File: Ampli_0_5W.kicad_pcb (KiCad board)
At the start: 2 copper layers, 100 x 100 mm, 66 parts, among them J1 RF_In, J2 PTT_In, J3 Aux_PTT_Out, J4 RF_Out, Q1 2N7002, Q2 FDD6685, Q3 2N5109, Q4 AFT05MP075N, T1 4:1, T2 1:1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

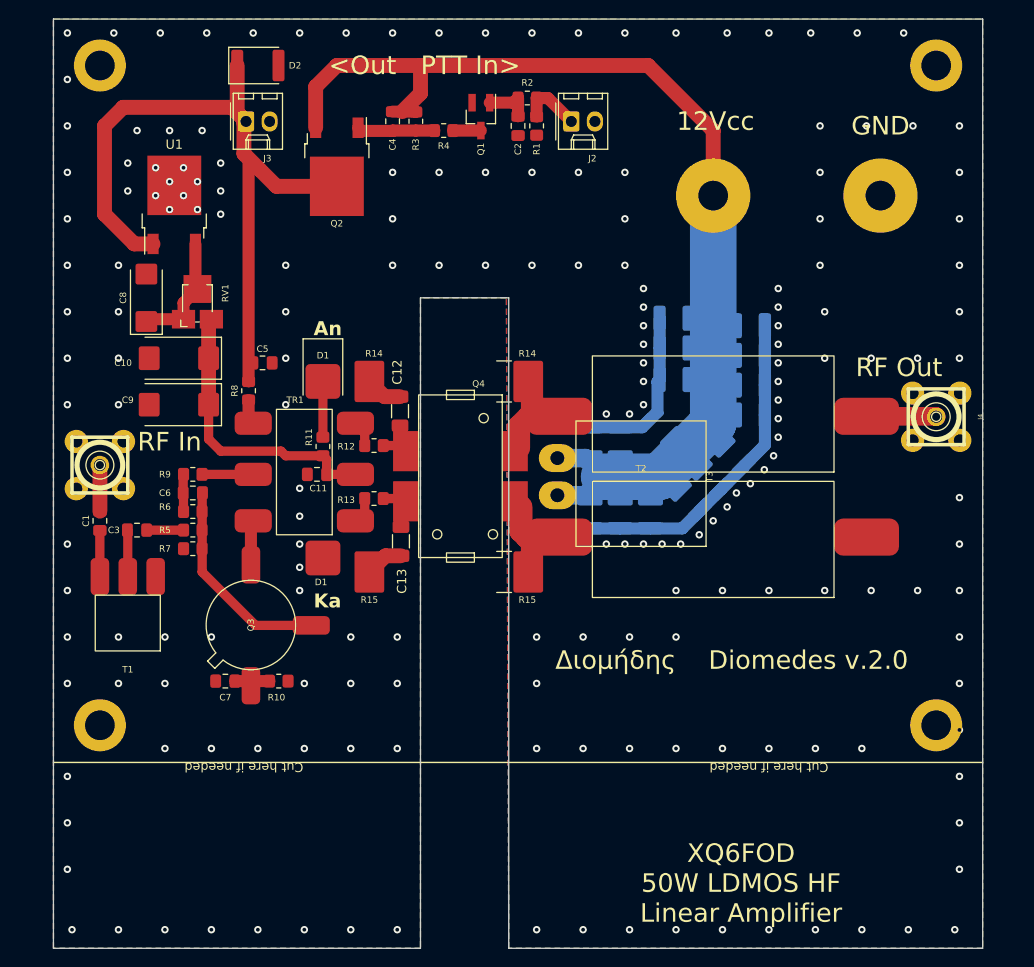
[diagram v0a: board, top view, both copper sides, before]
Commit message: pennywhistle compatible mounting holes
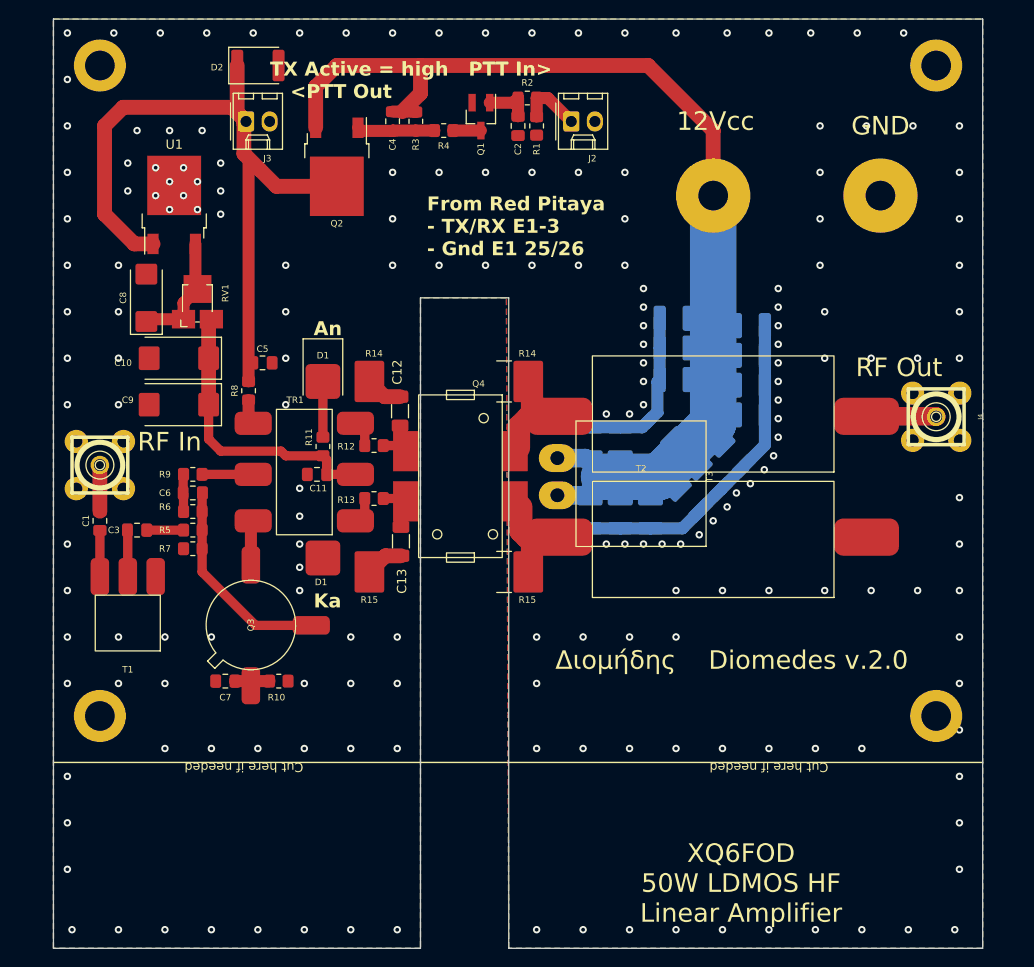
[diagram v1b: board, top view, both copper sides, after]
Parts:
- moved H4 1.00 mm to (85.0, 105.0)
- moved H6 1.00 mm to (175.0, 105.0)
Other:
- board text added: "From Red Pitaya - TX/RX E1-3 - Gnd E1 25/26"
- board text added: "TX Active = high PTT In> <PTT Out"
- board text removed: "<Out PTT In>"
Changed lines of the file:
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@@
   )
   (footprint "MountingHole:MountingHole_3.2mm_M3_DIN965_Pad" (layer "F.Cu")
-    (at 85 106)
+    (at 85 105)
     (descr "Mounting Hole 3.2mm, M3, DIN965")
     (tags "mounting hole 3.2mm m3 din965")
@@
     (property "ki_keywords" "diode")
     (attr smd)
-    (fp_text reference "D2" (at 4 0) (layer "F.SilkS")
+    (fp_text reference "D2" (at -4.4 0.2) (layer "F.SilkS")
         (effects (font (size 0.7 0.7) (thickness 0.15)))
     )
@@
   )
   (footprint "MountingHole:MountingHole_3.2mm_M3_DIN965_Pad" (layer "F.Cu")
-    (at 175 106)
+    (at 175 105)
     (descr "Mounting Hole 3.2mm, M3, DIN965")
     (tags "mounting hole 3.2mm m3 din965")
@@
     (effects (font (size 0.7 0.7) (thickness 0.15)))
   )
-  (gr_text " <Out   PTT In>" (at 119.5 35) (layer "F.SilkS")
-    (effects (font (size 2 2) (thickness 0.375)))
+  (gr_text "                      TX Active = high   PTT In>\n <PTT Out  " (at 110.6 36.6) (layer "F.SilkS")
+    (effects (font (size 1.5 1.5) (thickness 0.3) bold))
   )
   (gr_text "RF Out" (at 171 67.5) (layer "F.SilkS")
@@
     (effects (font (size 2 2) (thickness 0.4)))
   )
+  (gr_text "From Red Pitaya \n- TX/RX E1-3\n- Gnd E1 25/26" (at 120.2 55.6) (layer "F.SilkS")
+    (effects (font (size 1.5 1.5) (thickness 0.3) bold) (justify left bottom))
+  )
   (gr_text "Cut here if needed" (at 100.5 110.5 180) (layer "F.SilkS")
     (effects (font (size 1 1) (thickness 0.15)))
@@
     (effects (font (size 2 2) (thickness 0.4)))
   )
-  (dimension (type aligned) (layer "B.Cu")
-    (pts (xy 128.9 130) (xy 129.1 100))
-    (height -3.996577)
-    (gr_text "30.0007 mm" (at 123.203552 114.961357 89.6180338) (layer "B.Cu")
-      (effects (font (size 1.5 1.5) (thickness 0.3)))
+  (dimension (type aligned) (layer "F.SilkS")
+    (pts (xy 175 35) (xy 175 105))
+    (height -20)
+    (gr_text "70.0000 mm" (at 193.85 70 90) (layer "F.SilkS")
+      (effects (font (size 1 1) (thickness 0.15)))
     )
     (format (prefix "") (suffix "") (units 3) (units_format 1) (precision 4))
-    (style (thickness 0.2) (arrow_length 1.27) (text_position_mode 0) (extension_height 0.58642) (extension_offset 0.5) keep_text_aligned)
-  )
-  (dimension (type aligned) (layer "B.Cu")
-    (pts (xy 129 130) (xy 180 130))
-    (height 5.2)
-    (gr_text "51.0000 mm" (at 154.5 133.4) (layer "B.Cu")
-      (effects (font (size 1.5 1.5) (thickness 0.3)))
+    (style (thickness 0.15) (arrow_length 1.27) (text_position_mode 0) (extension_height 0.58642) (extension_offset 0.5) keep_text_aligned)
+  )
+  (dimension (type aligned) (layer "F.SilkS")
+    (pts (xy 85 35) (xy 175 35))
+    (height -20)
+    (gr_text "90.0000 mm" (at 130 13.85) (layer "F.SilkS")
+      (effects (font (size 1 1) (thickness 0.15)))
     )
     (format (prefix "") (suffix "") (units 3) (units_format 1) (precision 4))
-    (style (thickness 0.2) (arrow_length 1.27) (text_position_mode 0) (extension_height 0.58642) (extension_offset 0.5) keep_text_aligned)
+    (style (thickness 0.15) (arrow_length 1.27) (text_position_mode 0) (extension_height 0.58642) (extension_offset 0.5) keep_text_aligned)
   )
   (segment (start 85 78) (end 85 82.9625) (width 1.6) (layer "F.Cu") (net 1))

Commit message: new 3D image, minor changes
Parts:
- added C30: 100n, Capacitor_SMD:C_0603_1608Metric_Pad1.08x0.95mm_HandSolder, F.Cu at (105.5, 92.5)
- added Q5: 2SC5551A, Package_TO_SOT_SMD:SOT-89-3, F.Cu at (101.0, 90.6)
- added R16: 10R, Resistor_SMD:R_0603_1608Metric_Pad0.98x0.95mm_HandSolder, F.Cu at (105.5, 91.0)
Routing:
- net Net-(Q3-B): track 22.6 -> 32.0 mm
- net Net-(Q3-C): track 4.85 -> 0.35 mm
- net Net-(Q5-E): track 0.00 -> 3.69 mm
- net GND: track 52.7 -> 54.9 mm, vias 185 -> 213

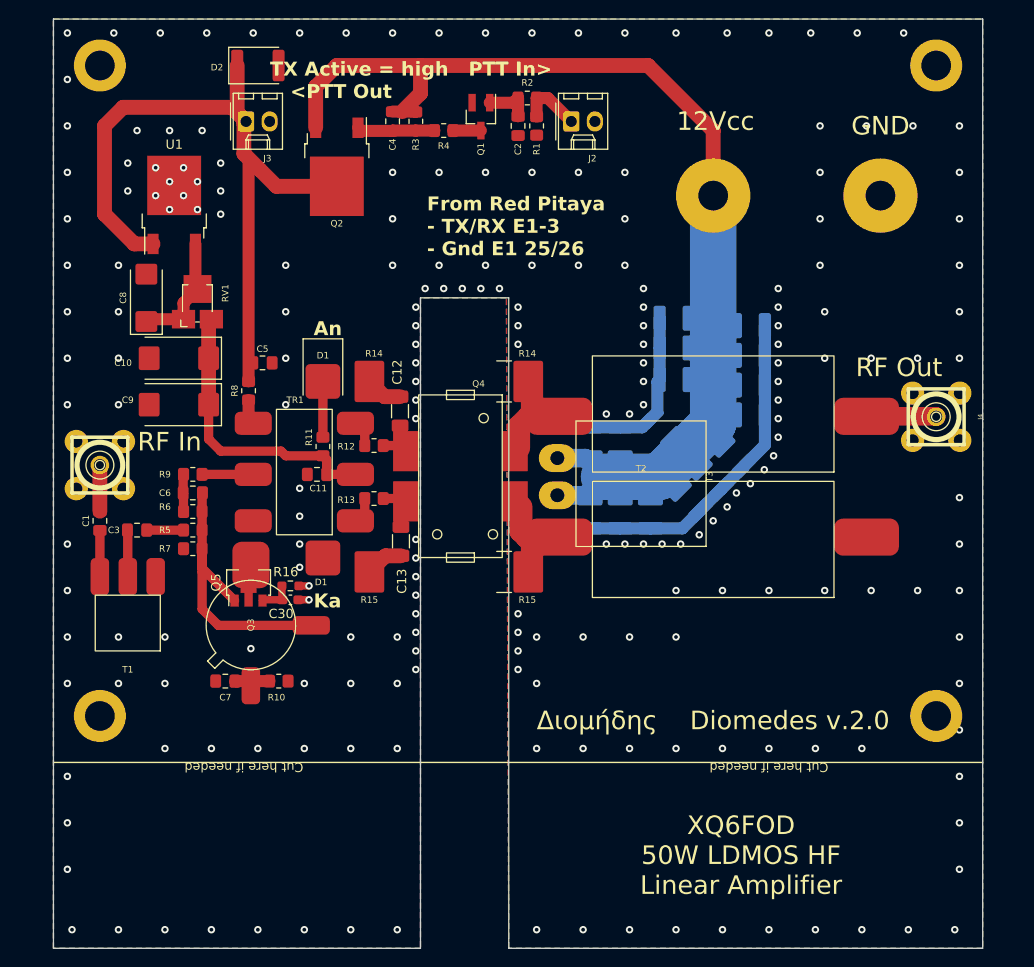
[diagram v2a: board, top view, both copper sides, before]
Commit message: new slotted pcb, new transistor added
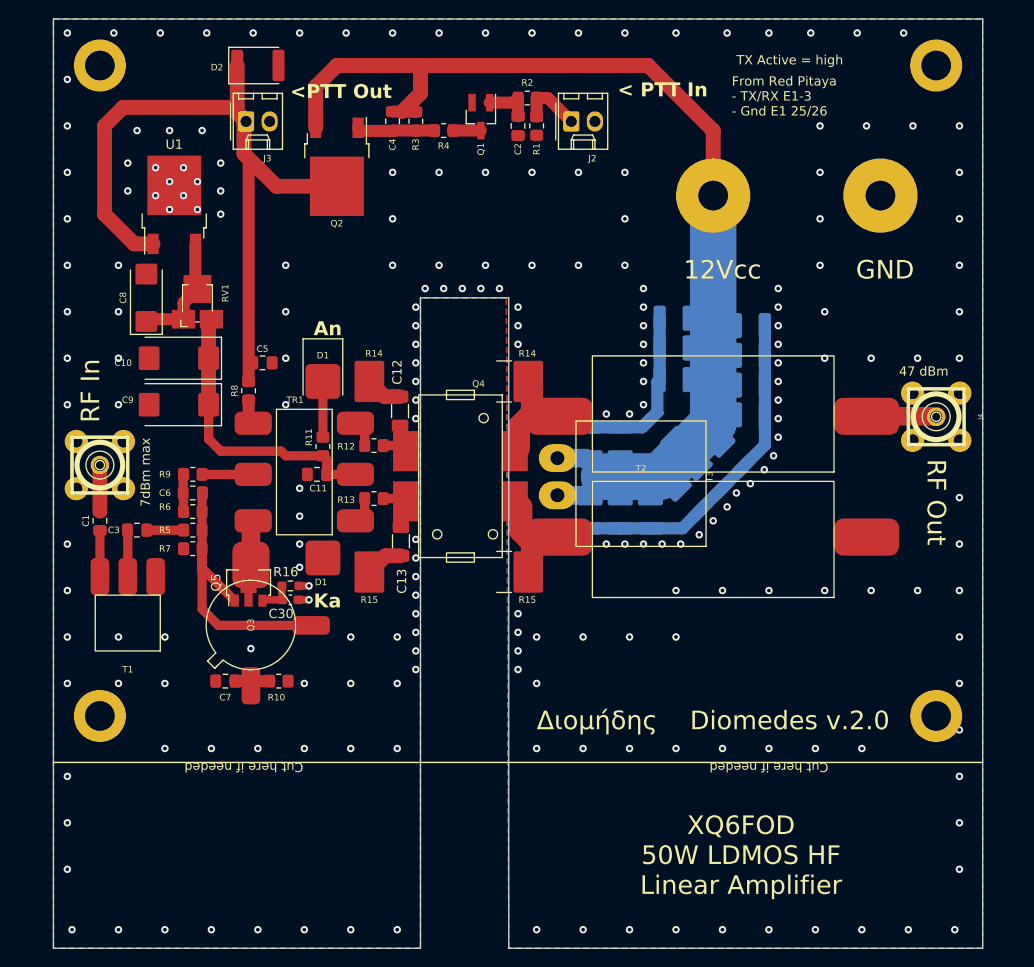
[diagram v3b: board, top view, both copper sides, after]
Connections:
- Q5 pad 2: unconnected-(Q5-C-Pad2) -> Net-(Q3-C)
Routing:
- net Net-(Q3-C): track 0.35 -> 4.85 mm
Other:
- board text added: "47 dBm"
- board text added: "7dBm max"
- board text added: "< PTT In"
- board text added: "<PTT Out"
- board text added: "TX Active = high"
- board text removed: "TX Active = high PTT In> <PTT Out"
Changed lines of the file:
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@@
   (net 27 "Net-(R12-Pad2)")
   (net 28 "Net-(R13-Pad2)")
-  (net 29 "unconnected-(Q5-C-Pad2)")
-  (net 30 "Net-(Q5-E)")
+  (net 29 "Net-(Q5-E)")
   (footprint "Capacitor_SMD:C_0603_1608Metric_Pad1.08x0.95mm_HandSolder" (layer "F.Cu")
     (at 105.5 92.5 180)
@@
       (net 2 "GND") (pintype "passive"))
     (pad "2" smd roundrect (at 0.8625 0 180) (size 1.075 0.95) (layers "F.Cu" "F.Paste" "F.Mask") (roundrect_rratio 0.25)
-      (net 30 "Net-(Q5-E)") (pintype "passive"))
+      (net 29 "Net-(Q5-E)") (pintype "passive"))
     (model "${KICAD6_3DMODEL_DIR}/Capacitor_SMD.3dshapes/C_0603_1608Metric.wrl"
       (offset (xyz 0 0 0))
@@
       (net 2 "GND") (pintype "passive"))
     (pad "2" smd roundrect (at 0.9125 0 180) (size 0.975 0.95) (layers "F.Cu" "F.Paste" "F.Mask") (roundrect_rratio 0.25)
-      (net 30 "Net-(Q5-E)") (pintype "passive"))
+      (net 29 "Net-(Q5-E)") (pintype "passive"))
     (model "${KICAD6_3DMODEL_DIR}/Resistor_SMD.3dshapes/R_0603_1608Metric.wrl"
       (offset (xyz 0 0 0))
@@
       (net 10 "Net-(Q3-B)") (pinfunction "B") (pintype "input"))
     (pad "2" smd custom (at -1.8625 0 90) (size 1.475 0.9) (layers "F.Cu" "F.Paste" "F.Mask")
-      (net 29 "unconnected-(Q5-C-Pad2)") (pinfunction "C") (pintype "passive") (zone_connect 2) (thermal_bridge_angle 45)
+      (net 23 "Net-(Q3-C)") (pinfunction "C") (pintype "passive") (zone_connect 2) (thermal_bridge_angle 45)
       (options (clearance outline) (anchor rect))
       (primitives
@@
       ))
     (pad "3" smd rect (at -1.95 1.5 90) (size 1.3 0.9) (layers "F.Cu" "F.Paste" "F.Mask")
-      (net 30 "Net-(Q5-E)") (pinfunction "E") (pintype "passive"))
+      (net 29 "Net-(Q5-E)") (pinfunction "E") (pintype "passive"))
     (model "${KICAD6_3DMODEL_DIR}/Package_TO_SOT_SMD.3dshapes/SOT-89-3.wrl"
       (offset (xyz 0 0 0))
@@
   (gr_line (start 129 60) (end 119.5 60)
     (stroke (width 0.1) (type solid)) (layer "Edge.Cuts"))
+  (gr_text "TX Active = high  " (at 153.5 35) (layer "F.SilkS")
+    (effects (font (size 1 1) (thickness 0.15)) (justify left bottom))
+  )
+  (gr_text "47 dBm" (at 171 68.5) (layer "F.SilkS")
+    (effects (font (size 1 1) (thickness 0.15)) (justify left bottom))
+  )
+  (gr_text " < PTT In" (at 140 38.5) (layer "F.SilkS")
+    (effects (font (size 1.5 1.5) (thickness 0.3) bold) (justify left bottom))
+  )
   (gr_text "D1" (at 108.8 90.6) (layer "F.SilkS")
     (effects (font (size 0.7 0.7) (thickness 0.15)))
   )
-  (gr_text "                      TX Active = high   PTT In>\n <PTT Out  " (at 110.6 36.6) (layer "F.SilkS")
+  (gr_text "7dBm max" (at 90.5 82.5 90) (layer "F.SilkS")
+    (effects (font (size 1 1) (thickness 0.15)) (justify left bottom))
+  )
+  (gr_text "\n <PTT Out  " (at 110.6 36.6) (layer "F.SilkS")
     (effects (font (size 1.5 1.5) (thickness 0.3) bold))
   )
-  (gr_text "RF Out" (at 171 67.5) (layer "F.SilkS")
+  (gr_text "RF Out" (at 175 82 -90) (layer "F.SilkS")
     (effects (font (size 2 2) (thickness 0.4)))
   )
@@
     (effects (font (size 2 2) (thickness 0.4)))
   )
-  (gr_text "From Red Pitaya \n- TX/RX E1-3\n- Gnd E1 25/26" (at 120.2 55.6) (layer "F.SilkS")
-    (effects (font (size 1.5 1.5) (thickness 0.3) bold) (justify left bottom))
+  (gr_text "From Red Pitaya \n- TX/RX E1-3\n- Gnd E1 25/26" (at 153 40.5) (layer "F.SilkS")
+    (effects (font (size 1 1) (thickness 0.15)) (justify left bottom))
   )
   (gr_text "Cut here if needed" (at 100.5 110.5 180) (layer "F.SilkS")
@@
     (effects (font (size 0.7 0.7) (thickness 0.15)))
   )
-  (gr_text "RF In" (at 92.5 75.5) (layer "F.SilkS")
+  (gr_text "RF In" (at 84 70 90) (layer "F.SilkS")
     (effects (font (size 2 2) (thickness 0.4)))
   )
-  (gr_text "12Vcc" (at 151.25 41) (layer "F.SilkS")
+  (gr_text "12Vcc" (at 152 57) (layer "F.SilkS")
     (effects (font (size 2 2) (thickness 0.4)))
   )
@@
     (effects (font (size 2 2) (thickness 0.4)))
   )
-  (gr_text "GND" (at 169 41.5) (layer "F.SilkS")
+  (gr_text "GND" (at 169.5 57) (layer "F.SilkS")
     (effects (font (size 2 2) (thickness 0.4)))
   )
@@
   (segment (start 126 42) (end 123 42) (width 1.3) (layer "F.Cu") (net 22))
   (segment (start 101.25 84.25) (end 101.5 84) (width 1.3) (layer "F.Cu") (net 23))
+  (segment (start 101.25 88.75) (end 101.25 84.25) (width 2) (layer "F.Cu") (net 23))
   (segment (start 131.1 69) (end 131.1 72.9) (width 1.6) (layer "F.Cu") (net 24))
   (segment (start 131.1 89.5) (end 131.1 85.85) (width 1.6) (layer "F.Cu") (net 24))
@@
   (segment (start 113.5 83) (end 112.5 84) (width 1) (layer "F.Cu") (net 28))
   (segment (start 113.5 81.6) (end 113.5 83) (width 1) (layer "F.Cu") (net 28))
-  (segment (start 104.5875 91) (end 104.5875 92.45) (width 0.8) (layer "F.Cu") (net 30))
-  (segment (start 104.5875 92.45) (end 104.6375 92.5) (width 0.8) (layer "F.Cu") (net 30))
-  (segment (start 102.5875 92.5) (end 102.5 92.5875) (width 0.8) (layer "F.Cu") (net 30))
-  (segment (start 104.6375 92.5) (end 102.5875 92.5) (width 0.8) (layer "F.Cu") (net 30))
+  (segment (start 104.5875 91) (end 104.5875 92.45) (width 0.8) (layer "F.Cu") (net 29))
+  (segment (start 104.5875 92.45) (end 104.6375 92.5) (width 0.8) (layer "F.Cu") (net 29))
+  (segment (start 102.5875 92.5) (end 102.5 92.5875) (width 0.8) (layer "F.Cu") (net 29))
+  (segment (start 104.6375 92.5) (end 102.5875 92.5) (width 0.8) (layer "F.Cu") (net 29))
   (zone (net 2) (net_name "GND") (layer "F.Cu") (hatch edge 0.508)
     (connect_pads yes (clearance 0.508))
